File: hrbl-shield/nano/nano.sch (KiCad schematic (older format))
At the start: 64 parts, among them P1 Digital, P2 Analog, U1 SFH6206-3T, U10 SFH6206-3T, U11 SFH6206-3T, U12 SFH6206-3T, U13 SFH6206-3T, U14 SFH6206-3T, U15 IFX27001TFV50ATMA1CT-ND, U16 SFH6206-3T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

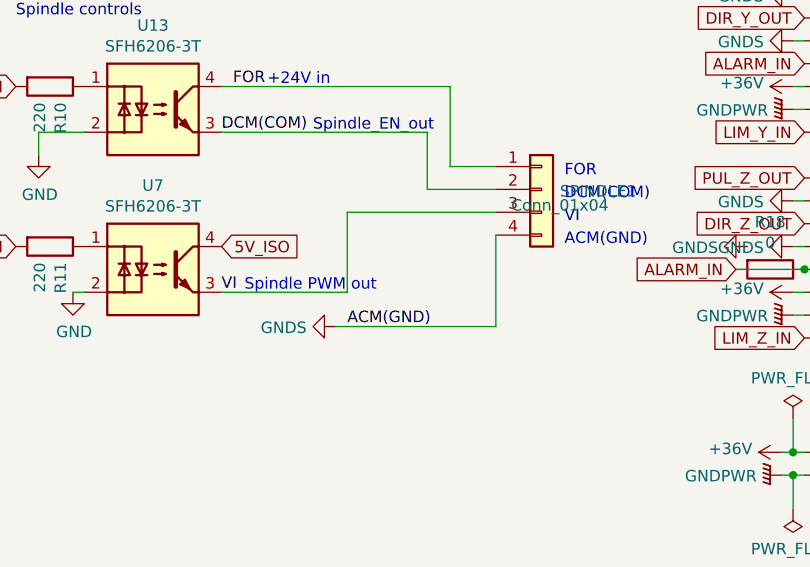
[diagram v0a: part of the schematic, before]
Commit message: Post for Grbl in fusion360 and nano PCB notes
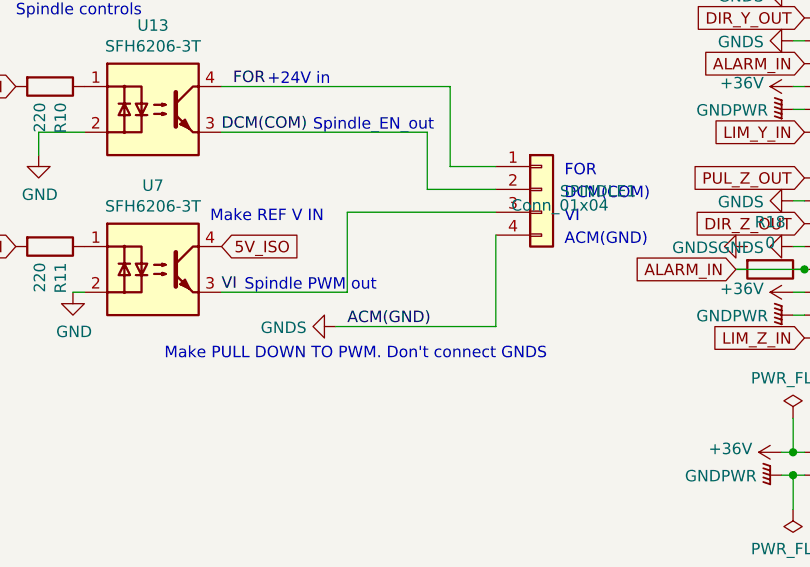
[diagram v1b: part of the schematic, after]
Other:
- note added: "Make PULL DOWN TO PWM. Don't connect GNDS"
- note added: "Make REF V IN"
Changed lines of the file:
@@
 Text Notes 3500 3200 0    50   ~ 0
 GRBL PINOUT REFERENCE
+Text Notes 6700 6550 0    50   ~ 0
+Make REF V IN
+Text Notes 6500 7150 0    50   ~ 0
+Make PULL DOWN TO PWM. Don't connect GNDS
 $EndSCHEMATC

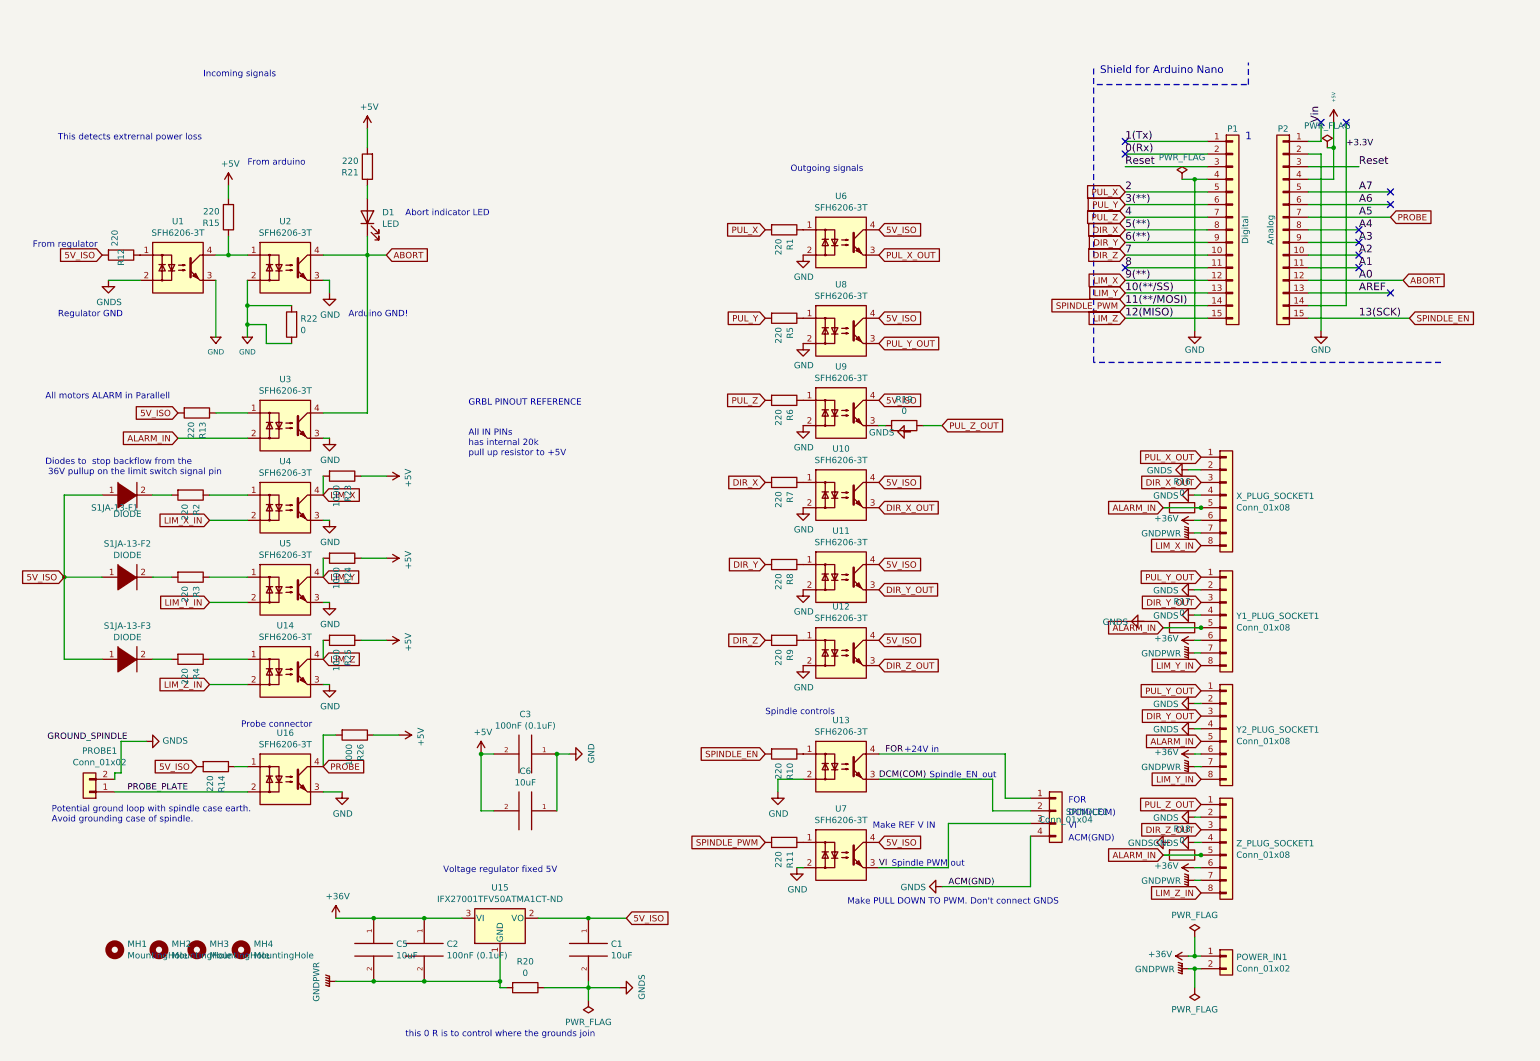
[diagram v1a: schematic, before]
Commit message: hrbl shield updated and folder cleaned
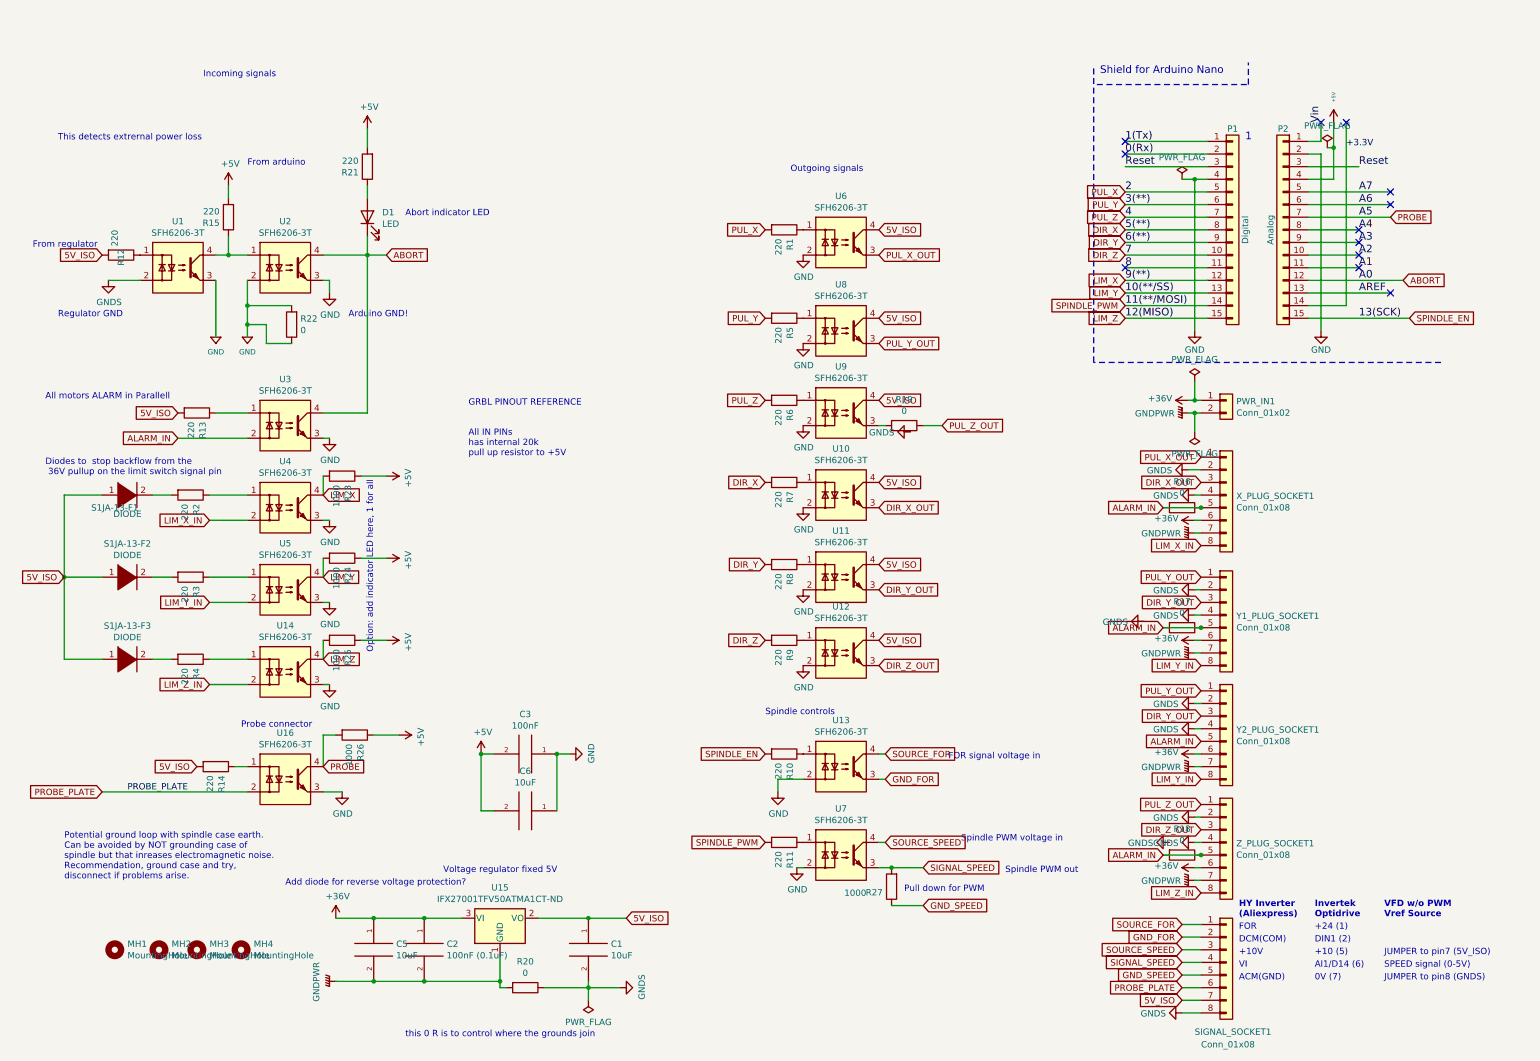
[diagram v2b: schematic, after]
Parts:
- removed PROBE1: Conn_01x02, Connector_Phoenix_MC:PhoenixContact_MCV_1,5_2-G-3.5_1x02_P3.50mm_Vertical, symbol Connector_Generic:Conn_01x02
- removed SPINDLE1: Conn_01x04, Connector_Phoenix_MC:PhoenixContact_MCV_1,5_4-G-3.5_1x04_P3.50mm_Vertical, symbol Connector_Generic:Conn_01x04
- added R27: 1000, Resistor_SMD:R_1206_3216Metric_Pad1.42x1.75mm_HandSolder, symbol Device:R
- added SIGNAL_SOCKET1: Conn_01x08, Connector_Phoenix_MC:PhoenixContact_MCV_1,5_8-G-3.5_1x08_P3.50mm_Vertical, symbol Connector_Generic:Conn_01x08
- C3: value 100nF (0.1uF) -> 100nF
- renumbered POWER_IN1 to PWR_IN1
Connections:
- net 5V_ISO: now also SIGNAL_SOCKET1.7 (Pin_7); no longer U7.4
- net GNDS: now also SIGNAL_SOCKET1.8 (Pin_8)
- net PROBE_PLATE: now also SIGNAL_SOCKET1.6 (Pin_6)
- net DCM(COM) renamed GND_FOR
- net GND_FOR: now also SIGNAL_SOCKET1.2 (Pin_2)
- net FOR renamed SOURCE_FOR
- net SOURCE_FOR: now also SIGNAL_SOCKET1.1 (Pin_1)
- net VI renamed SIGNAL_SPEED
- net SIGNAL_SPEED: now also R27.2, SIGNAL_SOCKET1.4 (Pin_4)
- new net GND_SPEED: R27.1, SIGNAL_SOCKET1.5 (Pin_5)
- new net SOURCE_SPEED: SIGNAL_SOCKET1.3 (Pin_3), U7.4
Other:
- note added: "+10 (5)"
- note added: "+10V"
- note added: "+24 (1)\n"
- note added: "0V (7)"
- note added: "Add diode for reverse voltage protection?"
- note added: "Al1/D14 (6)"
- note added: "DIN1 (2)"
- note added: "FOR signal voltage in"
- note added: "HY Inverter \n(Aliexpress)"
- note added: "Invertek\nOptidrive"
- note added: "JUMPER to pin7 (5V_ISO)"
- note added: "JUMPER to pin8 (GNDS)"
- note added: "Option: add indicator LED here, 1 for all"
- note added: "Potential ground loop with spindle case earth. \nCan be avoided by NOT grounding case of \nspindle but that inreases electromagnetic noise. \nRecommendation, ground case and try, \ndisconnect if problems arise."
- note added: "Pull down for PWM"
- note added: "SPEED signal (0-5V)"
- note added: "Spindle PWM voltage in"
- note added: "VFD w/o PWM\nVref Source"
- note added: "VI"
- note removed: "+24V in"
- note removed: "Make PULL DOWN TO PWM. Don't connect GNDS"
- note removed: "Make REF V IN"
- note removed: "Potential ground loop with spindle case earth. \nAvoid grounding case of spindle."
- note removed: "Spindle_EN_out"
- note removed: "VI\n"
- moved on the sheet: PWR_IN1

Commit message: Added spindle fault Abort to old card
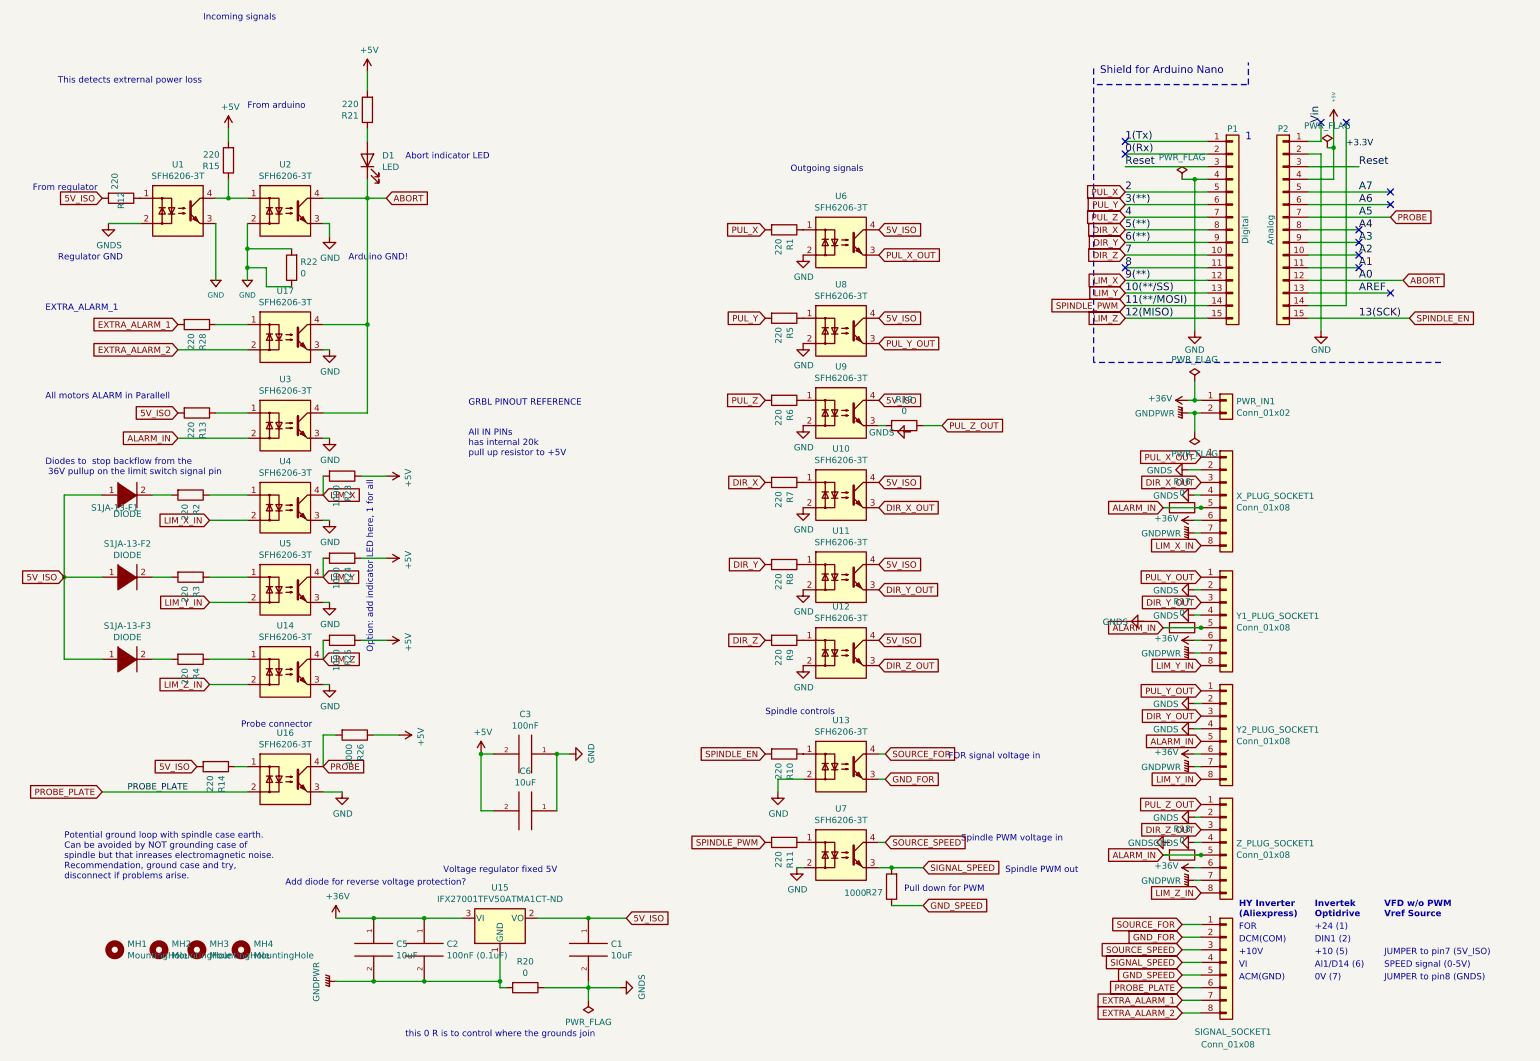
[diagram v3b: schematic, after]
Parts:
- added R28: 220, Resistor_SMD:R_1206_3216Metric_Pad1.42x1.75mm_HandSolder, symbol Device:R
- added U17: SFH6206-3T, Package_DIP:SMDIP-4_W9.53mm_Clearance8mm, symbol Isolator:SFH6206-3T
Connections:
- net 5V_ISO: no longer SIGNAL_SOCKET1.7 (Pin_7)
- net ABORT: now also U17.4
- net GND: now also U17.3
- net GNDS: no longer SIGNAL_SOCKET1.8 (Pin_8)
- new net: R28.1, U17.1
- new net EXTRA_ALARM_1: R28.2, SIGNAL_SOCKET1.7 (Pin_7)
- new net EXTRA_ALARM_2: SIGNAL_SOCKET1.8 (Pin_8), U17.2
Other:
- note added: "EXTRA_ALARM_1\n"
- moved on the sheet: D1, R12, R15, R21, R22, U1, U2
